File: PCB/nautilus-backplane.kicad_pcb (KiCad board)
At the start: 4 copper layers, 130.2 x 60.1 mm, 97 parts, among them J1 DE9_Socket_MountingHoles, J18 615008138321, J2 24.245.2, J3 24.245.2, J4 24.245.2, J5 24.245.2, J8 EdgeConn_Full, J9 643280100305

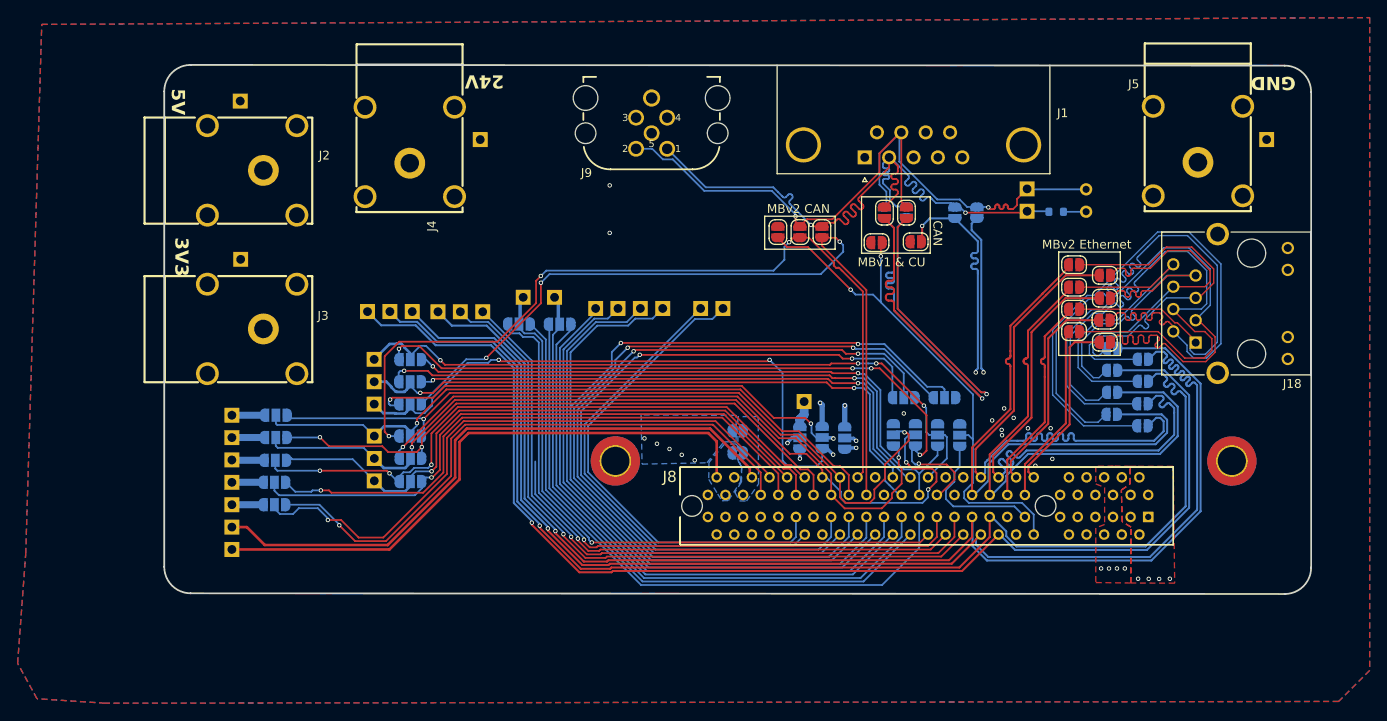
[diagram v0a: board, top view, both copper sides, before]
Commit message: Added info on silkscreen
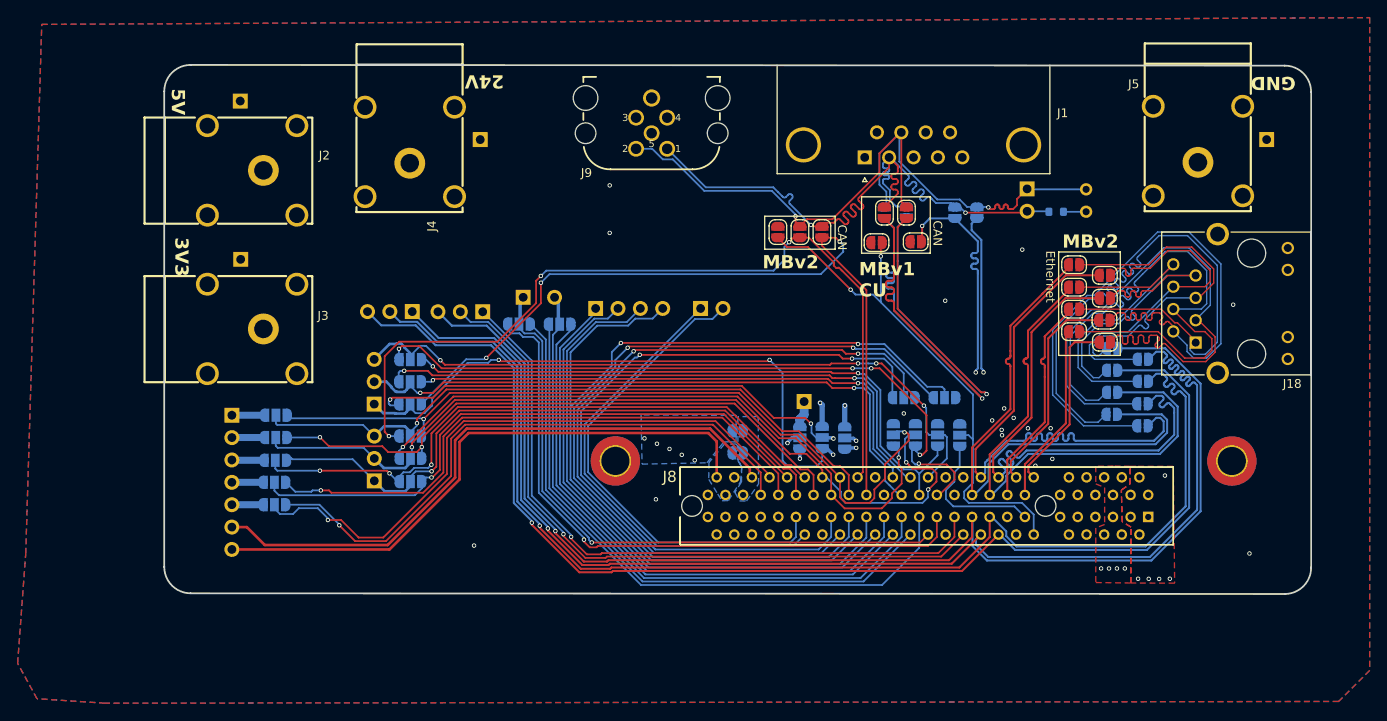
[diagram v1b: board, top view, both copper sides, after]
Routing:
- net /A22: track 54.0 -> 0.00 mm, vias 1 -> 0
- net GND: vias 12 -> 19
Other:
- board text added: "-M1-"
- board text added: "-M2-"
- board text added: "1"
- board text added: "11"
- board text added: "12"
- board text added: "2"
- board text added: "21"
- board text added: "22"
- board text added: "Battery pack voltages"
- board text added: "Ethernet"
- board text added: "H1"
- board text added: "H2"
- board text added: "H3"
- board text added: "Hall Sensors"
- board text added: "MBv1"
- board text added: "MBv1 CU"
- board text added: "MBv2"
- board text added: "Motor windings voltages"
- board text added: "N"
- board text added: "P1"
- board text added: "P2"
- board text added: "P3"
- board text added: "P4"
- board text added: "P5"
- board text added: "P6"
- board text added: "Valves"
- board text added: "W1"
- board text added: "W2"
- board text added: "W3"
- board text removed: "CU"
- board text removed: "MBv1 & CU"
- board text removed: "MBv1 Ethernet"
- board text removed: "MBv2 CAN"
- board text removed: "MBv2 Ethernet"

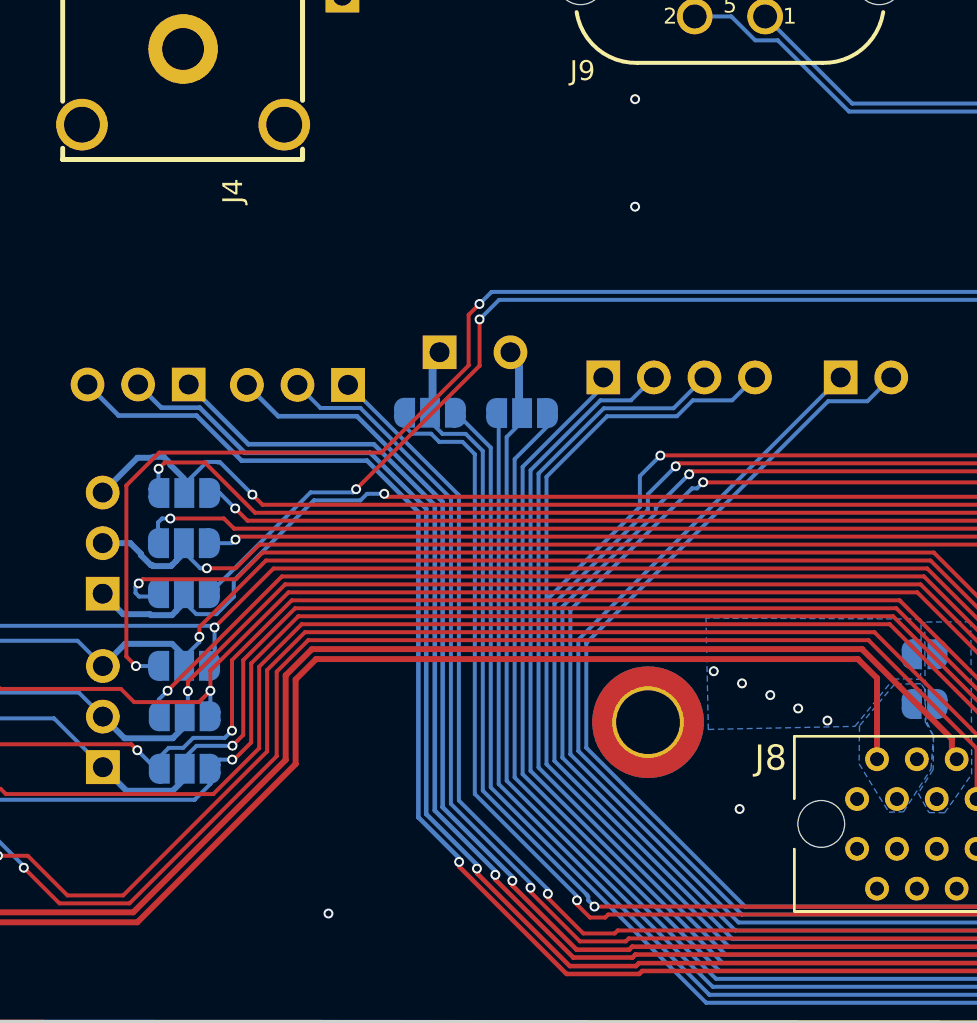
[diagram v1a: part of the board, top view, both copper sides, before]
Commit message: Added logos
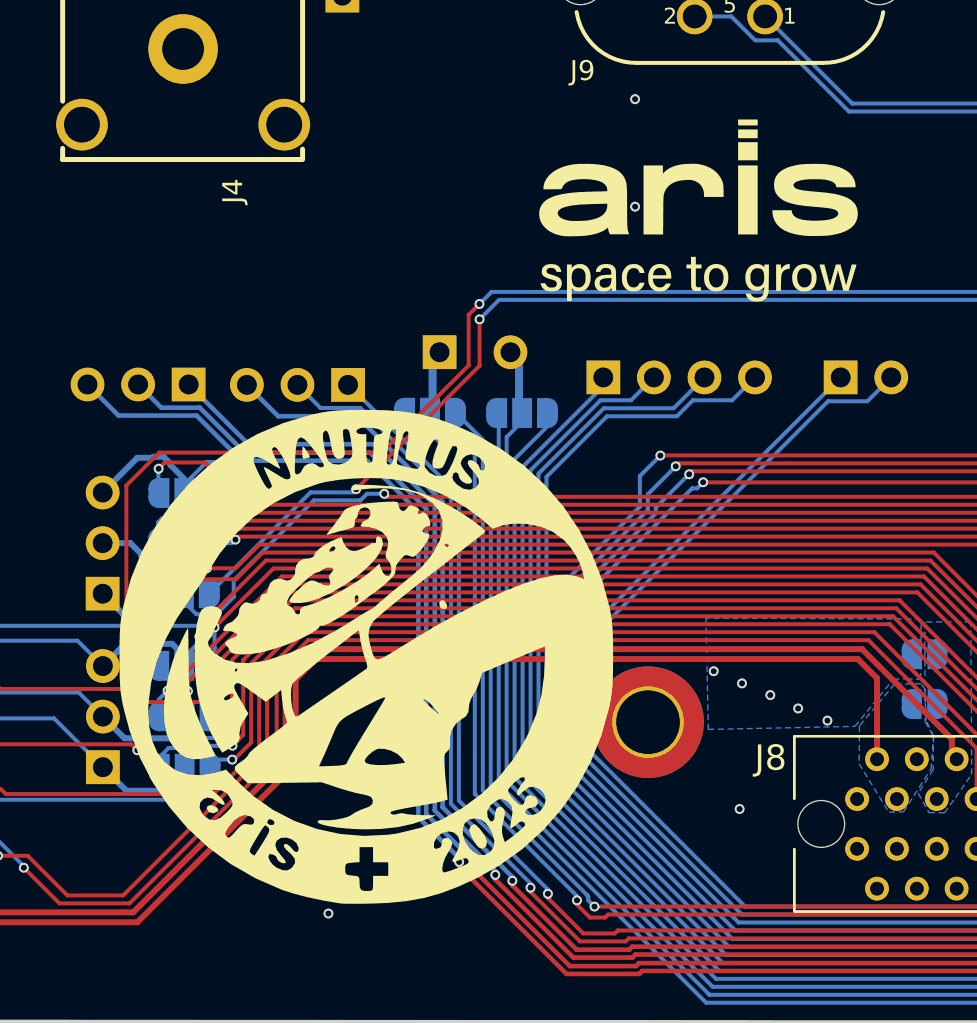
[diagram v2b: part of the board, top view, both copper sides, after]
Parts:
- added G***: LOGO, dz_art:aris_16mm_silk, F.Cu at (162.3, 90.2)
- added G***: LOGO, dz_art:NAUTILUS_logo, F.Cu at (145.6, 112.6)
- added G***: LOGO, dz_art:aris_16mm_silk, B.Cu at (140.5, 125.5)
